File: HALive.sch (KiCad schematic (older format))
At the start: 14 parts, among them J1 Screw_Terminal_01x08, J2 Conn_01x06_Male, J3 Conn_01x02_Male, J4 Screw_Terminal_01x08, J6 Conn_01x02_Male, U1 MAX233, U2 TMR_1-1211, U3 LM358

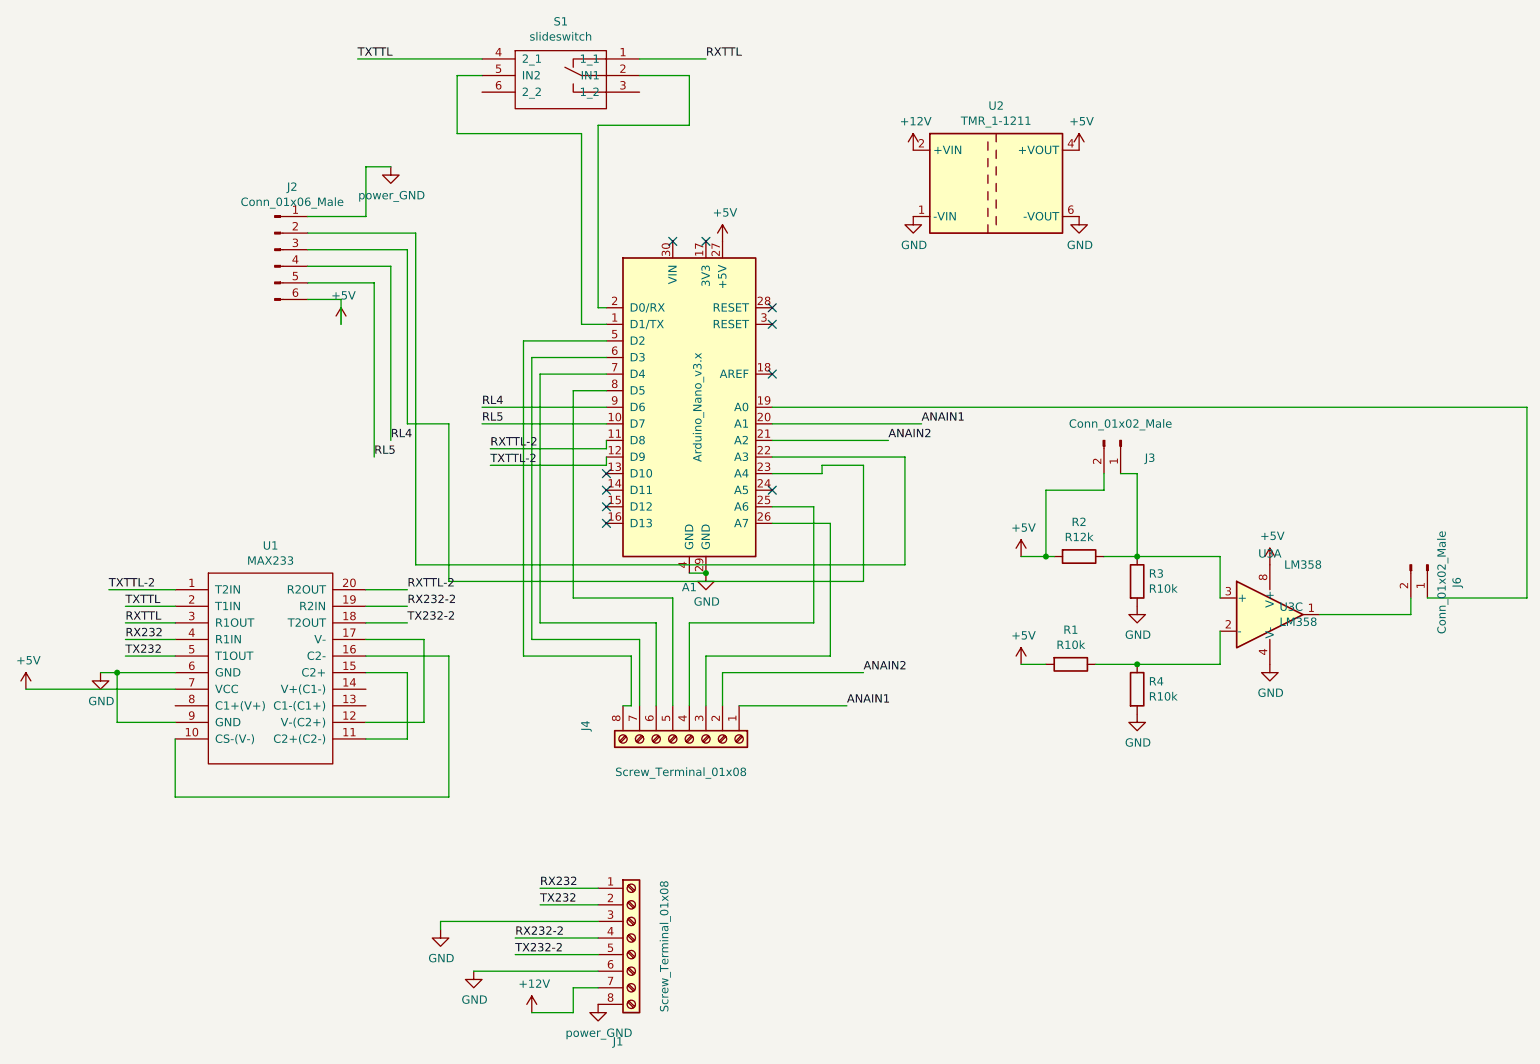
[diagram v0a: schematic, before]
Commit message: added BEM280 sensor
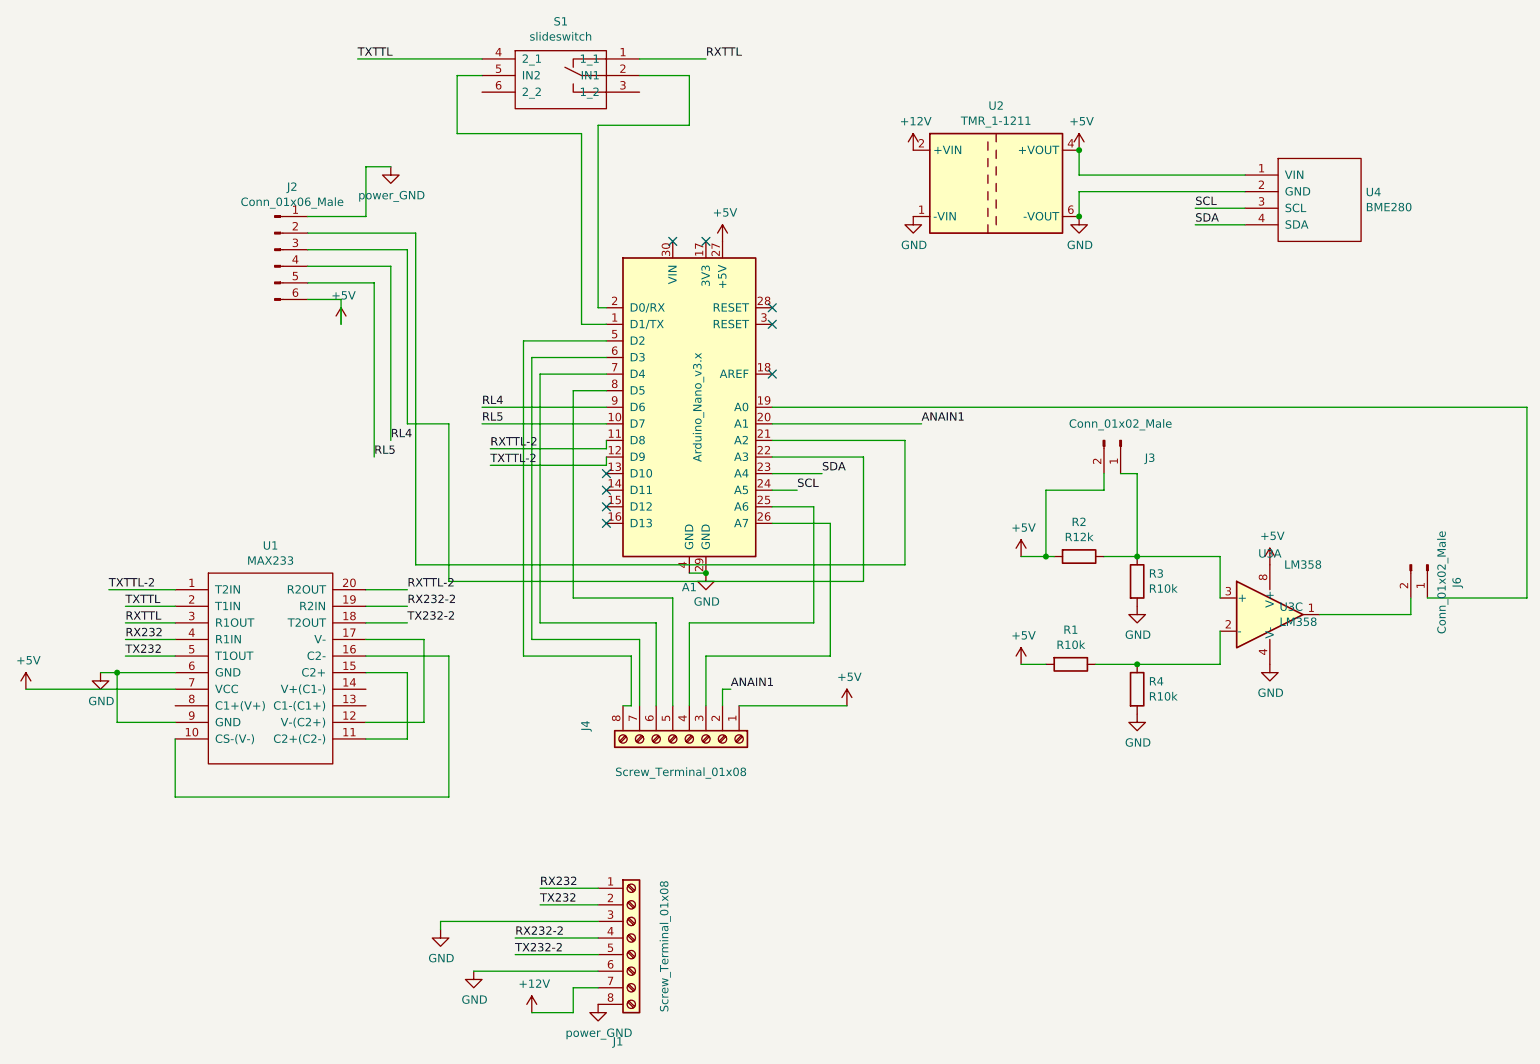
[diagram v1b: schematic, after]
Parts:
- added U4: BME280, lorenzo2018:BME280, symbol lorenzo2018:BME280
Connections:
- net +5V: now also J4.1 (Pin_1), U4.1 (VIN)
- net ANAIN1: now also J4.2 (Pin_2); no longer J4.1 (Pin_1)
- net GND: now also U4.2 (GND)
- net at J2.2 (Pin_2): now also A1.21 (A2); no longer A1.22 (A3)
- net at J2.3 (Pin_3): now also A1.22 (A3); no longer A1.23 (A4)
- net SCL: now reaches A1.24 (A5)
- net SCL: now also U4.3 (SCL)
- removed net ANAIN2: A1.21 (A2), J4.2 (Pin_2)
- new net SDA: A1.23 (A4), U4.4 (SDA)
- no-connect marks 10 -> 9
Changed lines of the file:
@@
 	6000 3100 6900 3100
-Wire Wire Line
-	6000 3200 6700 3200
 Wire Wire Line
 	5500 4300 6250 4300
@@
 NoConn ~ 6000 2500
 NoConn ~ 6000 2800
-NoConn ~ 6000 3500
 $Comp
 L lorenzo2018:MAX233 U1
@@
 Text Label 6900 3100 0    50   ~ 0
 ANAIN1
-Text Label 6700 3200 0    50   ~ 0
-ANAIN2
 Wire Wire Line
 	5300 4300 5300 4800
@@
 Wire Wire Line
 	5600 4800 5600 4500
-Wire Wire Line
-	5700 4800 5700 4600
-Wire Wire Line
-	5700 4600 6550 4600
-Text Label 6450 4800 0    50   ~ 0
+Text Label 5750 4700 0    50   ~ 0
 ANAIN1
-Text Label 6550 4600 0    50   ~ 0
-ANAIN2
 Text Label 4600 5900 0    50   ~ 0
 RX232
@@
 	3850 3950 6800 3950
 Wire Wire Line
-	6800 3950 6800 3300
-Wire Wire Line
 	3850 1950 3850 3950
 Wire Wire Line
-	6000 3300 6800 3300
-Wire Wire Line
-	6300 3350 6550 3350
-Wire Wire Line
-	6550 3350 6550 4050
-Wire Wire Line
 	6550 4050 4050 4050
 Wire Wire Line
@@
 Wire Wire Line
 	4050 3100 3800 3100
-Wire Wire Line
-	6300 3400 6300 3350
 Wire Wire Line
 	4250 3000 5000 3000
@@
 	0    1    1    0
 $EndComp
+$Comp
+L lorenzo2018:BME280 U4
+U 1 1 5D298D7A
+P 9250 1800
+F 0 "U4" H 9578 1896 50  0000 L CNN
+F 1 "BME280" H 9578 1805 50  0000 L CNN
+F 2 "lorenzo2018:BME280" H 9250 1800 50  0001 C CNN
+F 3 "" H 9250 1800 50  0001 C CNN
+	1    9250 1800
+	1    0    0    -1
+$EndComp
+Wire Wire Line
+	7850 1450 7850 1600
+Wire Wire Line
+	7850 1600 8850 1600
+Connection ~ 7850 1450
+Wire Wire Line
+	8850 1700 7850 1700
+Wire Wire Line
+	7850 1700 7850 1850
+Connection ~ 7850 1850
+Wire Wire Line
+	6000 3500 6150 3500
+Text Label 6150 3500 0    50   ~ 0
+SCL
+Text Label 6300 3400 0    50   ~ 0
+SDA
+Text Label 8550 1800 0    50   ~ 0
+SCL
+Text Label 8550 1900 0    50   ~ 0
+SDA
+Wire Wire Line
+	8850 1800 8550 1800
+Wire Wire Line
+	8850 1900 8550 1900
+Wire Wire Line
+	6000 3200 6800 3200
+Wire Wire Line
+	6800 3200 6800 3950
+Wire Wire Line
+	6000 3300 6550 3300
+Wire Wire Line
+	6550 3300 6550 4050
+Wire Wire Line
+	5700 4800 5700 4700
+Wire Wire Line
+	5700 4700 5750 4700
+$Comp
+L power:+5V #PWR?
+U 1 1 5D2A319A
+P 6450 4800
+F 0 "#PWR?" H 6450 4650 50  0001 C CNN
+F 1 "+5V" H 6465 4973 50  0000 C CNN
+F 2 "" H 6450 4800 50  0001 C CNN
+F 3 "" H 6450 4800 50  0001 C CNN
+	1    6450 4800
+	1    0    0    -1
+$EndComp
 $EndSCHEMATC
